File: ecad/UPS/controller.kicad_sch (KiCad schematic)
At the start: 32 parts, among them J4 Conn_01x05_Socket, SW1 SW_Push, SW2 SW_Push, U4 STM32L152RCT6, U5 AP2112K-3.3TRG1

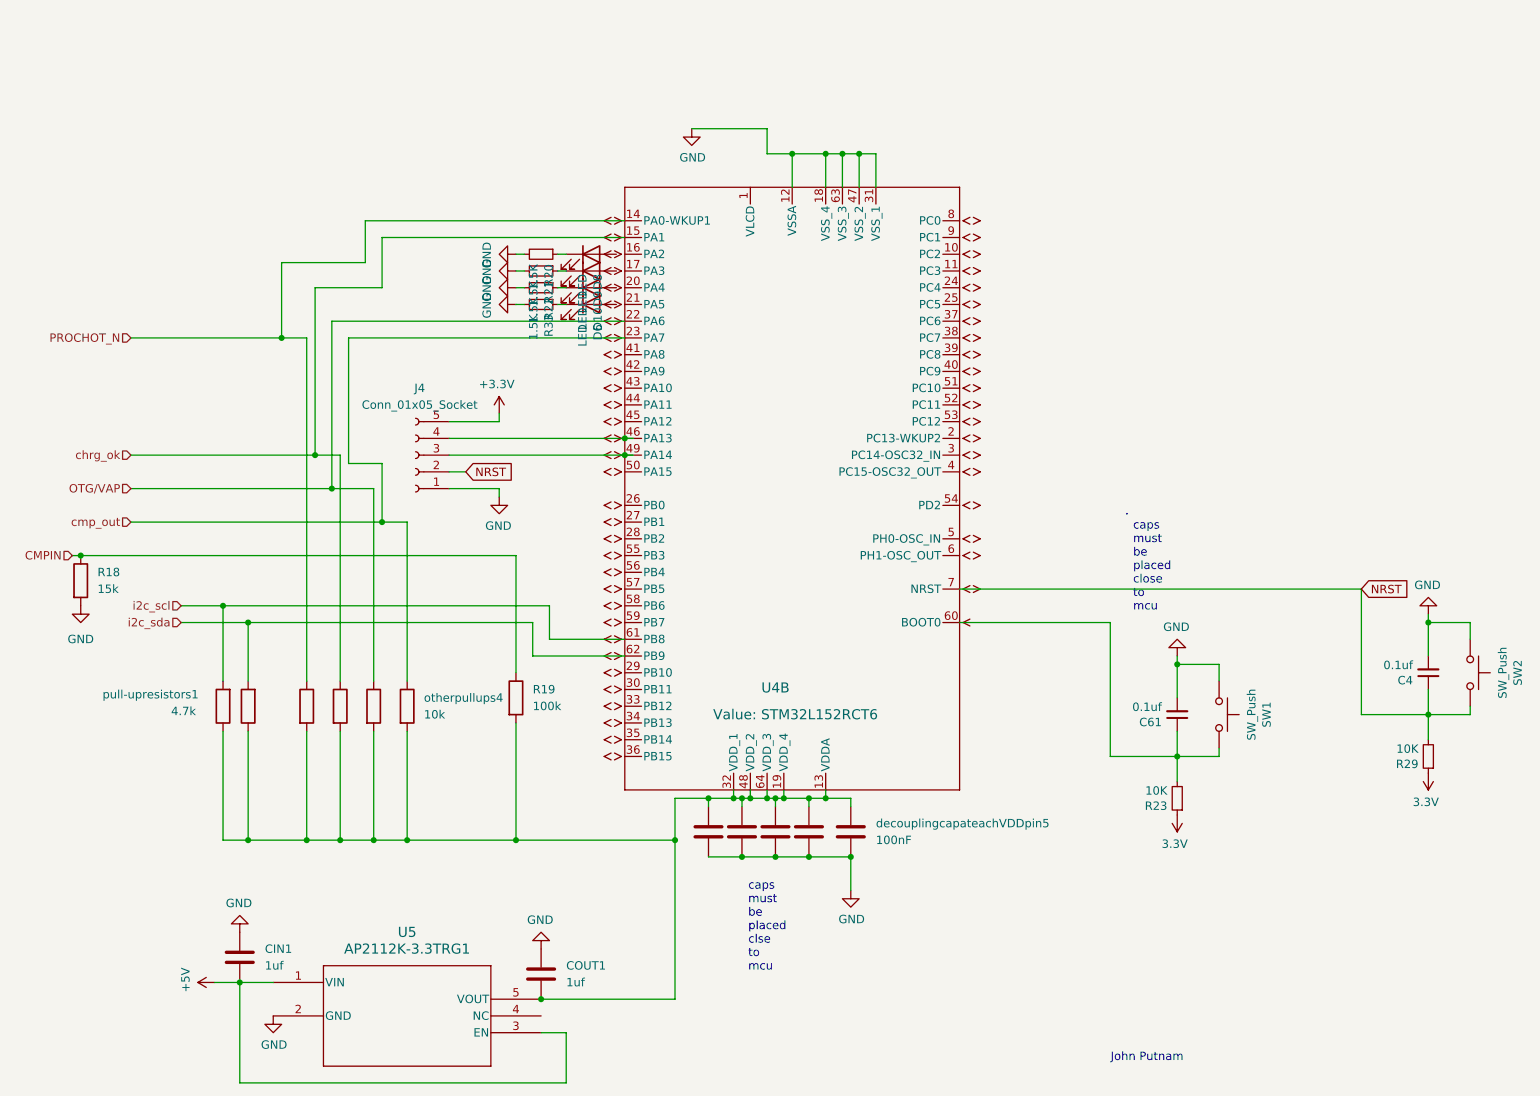
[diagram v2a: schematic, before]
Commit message: boot0 fix
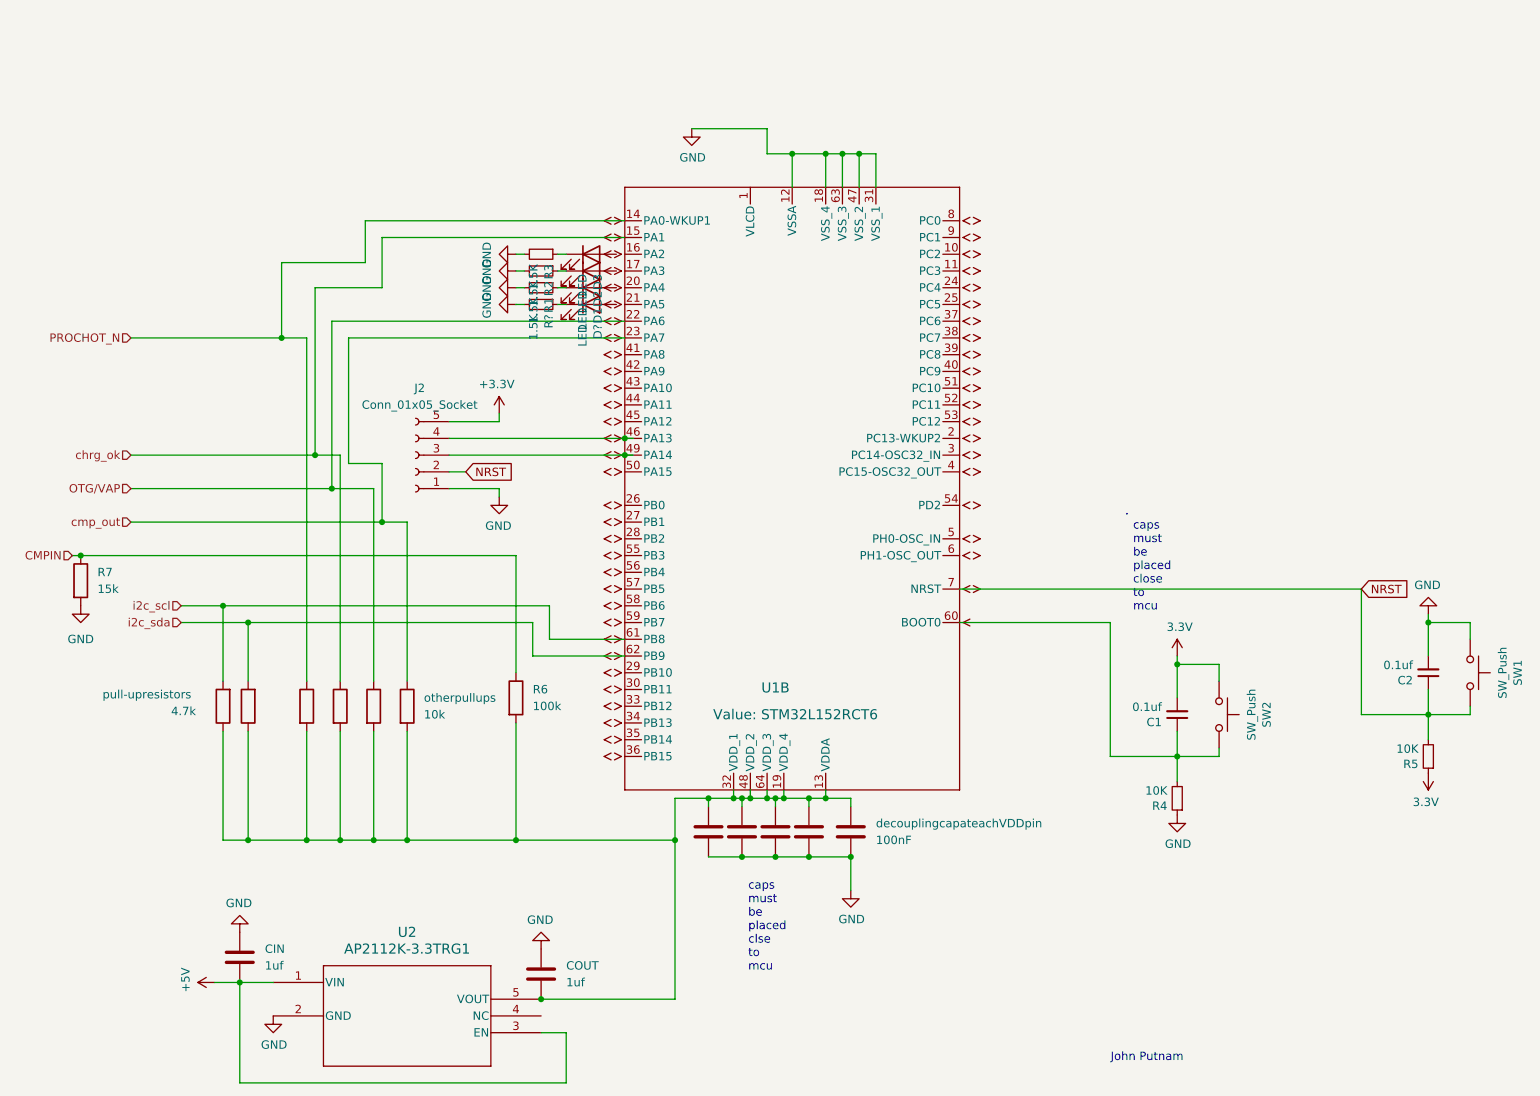
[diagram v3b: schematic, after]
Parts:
- renumbered C61 to C1, C4 to C2, CIN1 to CIN, COUT1 to COUT, D10 to D1, D9 to D2, D8 to D3, D6 to D?, J4 to J2, R22 to R1, R21 to R2, R20 to R3, R23 to R4, R29 to R5, R19 to R6, R18 to R7, R33 to R?, SW2 to SW1, SW1 to SW2, U4 to U1, U5 to U2, decouplingcapateachVDDpin5 to decouplingcapateachVDDpin, decouplingcapateachVDDpin4 to decouplingcapateachVDDpin1, decouplingcapateachVDDpin3 to decouplingcapateachVDDpin2, decouplingcapateachVDDpin2 to decouplingcapateachVDDpin3, decouplingcapateachVDDpin1 to decouplingcapateachVDDpin4, otherpullups4 to otherpullups, otherpullups3 to otherpullups1, otherpullups1 to otherpullups3, pull-upresistoronSDA1 to pull-upresistoronSDA, pull-upresistors1 to pull-upresistors
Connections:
- net 3.3V: now also C1.2, SW2.1; no longer R4.1
- net GND: now also R4.1; no longer C1.2, SW2.1
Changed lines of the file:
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@@
 		(on_board yes)
 		(dnp no)
-		(property "Reference" "#PWR0120"
+		(property "Reference" "#PWR030"
 			(at 87.63 78.74 0)
 			(effects
@@
 		(on_board yes)
 		(dnp no)
-		(property "Reference" "#PWR0126"
+		(property "Reference" "#PWR031"
 			(at 87.63 93.98 0)
 			(effects
@@
 		(on_board yes)
 		(dnp no)
-		(property "Reference" "#PWR0118"
+		(property "Reference" "#PWR012"
 			(at 48.26 161.29 0)
 			(effects
@@
 		(on_board yes)
 		(dnp no)
-		(property "Reference" "#PWR0119"
+		(property "Reference" "#PWR013"
 			(at 48.26 147.32 0)
 			(effects
@@
 		(on_board yes)
 		(dnp no)
-		(property "Reference" "#PWR0113"
+		(property "Reference" "#PWR04"
 			(at 228.6 125.73 0)
 			(effects
@@
 		(on_board yes)
 		(dnp no)
-		(property "Reference" "SW2"
+		(property "Reference" "SW1"
 			(at 242.189 114.3 0)
 			(effects
@@
 		(on_board yes)
 		(dnp no)
-		(property "Reference" "#PWR0114"
+		(property "Reference" "#PWR05"
 			(at 228.6 99.06 0)
 			(effects
@@
 		(on_board yes)
 		(dnp no)
-		(property "Reference" "#PWR0124"
+		(property "Reference" "#PWR024"
 			(at 83.82 58.42 0)
 			(effects
@@
 		(on_board yes)
 		(dnp no)
-		(property "Reference" "pull-upresistors1"
+		(property "Reference" "pull-upresistors"
 			(at 27.432 117.602 0)
 			(effects
@@
 		(on_board yes)
 		(dnp no)
-		(property "Reference" "D6"
+		(property "Reference" "D?"
 			(at 102.5906 61.4172 90)
 			(effects
@@
 		(dnp no)
 		(fields_autoplaced yes)
-		(property "Reference" "decouplingcapateachVDDpin4"
+		(property "Reference" "decouplingcapateachVDDpin1"
 			(at 138.43 137.1599 0)
 			(effects
@@
 		(on_board yes)
 		(dnp no)
-		(property "Reference" "C61"
+		(property "Reference" "C1"
 			(at 188.1632 121.8184 0)
 			(effects
@@
 		(on_board yes)
 		(dnp no)
-		(property "Reference" "R29"
+		(property "Reference" "R5"
 			(at 227.1014 128.1684 0)
 			(effects
@@
 		(on_board yes)
 		(dnp no)
-		(property "Reference" "R21"
+		(property "Reference" "R2"
 			(at 95.1484 54.8386 0)
 			(effects
@@
 		(on_board yes)
 		(dnp no)
-		(property "Reference" "D9"
+		(property "Reference" "D2"
 			(at 102.5906 56.3372 90)
 			(effects
@@
 		(dnp no)
 		(fields_autoplaced yes)
-		(property "Reference" "decouplingcapateachVDDpin5"
+		(property "Reference" "decouplingcapateachVDDpin"
 			(at 144.78 137.1599 0)
 			(effects
@@
 		(on_board yes)
 		(dnp no)
-		(property "Reference" "R33"
+		(property "Reference" "R?"
 			(at 95.1484 59.9186 0)
 			(effects
@@
 		(on_board yes)
 		(dnp no)
-		(property "Reference" "R22"
+		(property "Reference" "R1"
 			(at 95.1484 57.3786 0)
 			(effects
@@
 	(symbol
 		(lib_id "power:+3.3V")
-		(at 190.5 135.89 180)
+		(at 190.5 111.76 0)
 		(unit 1)
 		(exclude_from_sim no)
@@
 		(on_board yes)
 		(dnp no)
-		(property "Reference" "#PWR0110"
-			(at 190.5 132.08 0)
+		(property "Reference" "#PWR014"
+			(at 190.5 115.57 0)
 			(effects
 				(font
@@
 		)
 		(property "Value" "3.3V"
-			(at 190.119 140.2842 0)
+			(at 190.881 107.3658 0)
 			(effects
 				(font
@@
 		)
 		(property "Footprint" ""
-			(at 190.5 135.89 0)
+			(at 190.5 111.76 0)
 			(effects
 				(font
@@
 		)
 		(property "Datasheet" ""
-			(at 190.5 135.89 0)
+			(at 190.5 111.76 0)
 			(effects
 				(font
@@
 		)
 		(property "Description" ""
-			(at 190.5 135.89 0)
+			(at 190.5 111.76 0)
 			(effects
 				(font
@@
 				)
 			)
-			(project "UPS"
-				(path "/9d92b60a-4a6b-449c-b462-cab19e69d38c/1d606685-c4fd-4b8c-9a71-b1626d28c437"
-					(reference "#PWR0110")
-					(unit 1)
-				)
-			)
 		)
 	)
@@
 		(on_board yes)
 		(dnp no)
-		(property "Reference" "#PWR0121"
+		(property "Reference" "#PWR09"
 			(at 83.82 50.8 0)
 			(effects
@@
 		(dnp no)
 		(fields_autoplaced yes)
-		(property "Reference" "R18"
+		(property "Reference" "R7"
 			(at 26.67 99.0599 0)
 			(effects
@@
 		(on_board yes)
 		(dnp no)
-		(property "Reference" "#PWR0123"
+		(property "Reference" "#PWR07"
 			(at 83.82 55.88 0)
 			(effects
@@
 		(on_board yes)
 		(dnp no)
-		(property "Reference" "#PWR0111"
+		(property "Reference" "#PWR06"
 			(at 140.97 153.67 0)
 			(effects
@@
 		(dnp no)
 		(fields_autoplaced yes)
-		(property "Reference" "U5"
+		(property "Reference" "U2"
 			(at 73.66 153.67 0)
 			(effects
@@
 		(on_board yes)
 		(dnp no)
-		(property "Reference" "#PWR0125"
+		(property "Reference" "#PWR010"
 			(at 116.84 38.1 0)
 			(effects
@@
 		(on_board yes)
 		(dnp no)
-		(property "Reference" "SW1"
+		(property "Reference" "SW2"
 			(at 204.089 120.65 0)
 			(effects
@@
 		(on_board yes)
 		(dnp no)
-		(property "Reference" "#PWR0116"
+		(property "Reference" "#PWR02"
 			(at 53.34 172.72 0)
 			(effects
@@
 		(on_board yes)
 		(dnp no)
-		(property "Reference" "D8"
+		(property "Reference" "D3"
 			(at 102.5906 53.7972 90)
 			(effects
@@
 		(on_board yes)
 		(dnp no)
-		(property "Reference" "D10"
+		(property "Reference" "D1"
 			(at 102.5906 58.8772 90)
 			(effects
@@
 		(dnp no)
 		(fields_autoplaced yes)
-		(property "Reference" "otherpullups4"
+		(property "Reference" "otherpullups"
 			(at 76.2 118.1099 0)
 			(effects
@@
 		(dnp no)
 		(fields_autoplaced yes)
-		(property "Reference" "otherpullups3"
+		(property "Reference" "otherpullups1"
 			(at 71.12 118.1099 0)
 			(effects
@@
 		(dnp no)
 		(fields_autoplaced yes)
-		(property "Reference" "pull-upresistoronSDA1"
+		(property "Reference" "pull-upresistoronSDA"
 			(at 52.07 118.1099 0)
 			(effects
@@
 		(dnp no)
 		(fields_autoplaced yes)
-		(property "Reference" "J4"
+		(property "Reference" "J2"
 			(at 75.565 71.12 0)
 			(effects
@@
 		(dnp no)
 		(fields_autoplaced yes)
-		(property "Reference" "decouplingcapateachVDDpin2"
+		(property "Reference" "decouplingcapateachVDDpin3"
 			(at 128.27 137.1599 0)
 			(effects
@@
 		(on_board yes)
 		(dnp no)
-		(property "Reference" "R23"
+		(property "Reference" "R4"
 			(at 189.0014 134.5184 0)
 			(effects
@@
 	(symbol
 		(lib_id "power:GND")
-		(at 190.5 111.76 180)
+		(at 190.5 135.89 0)
 		(unit 1)
 		(exclude_from_sim no)
@@
 		(on_board yes)
 		(dnp no)
-		(property "Reference" "#PWR0112"
-			(at 190.5 105.41 0)
+		(property "Reference" "#PWR011"
+			(at 190.5 142.24 0)
 			(effects
 				(font
@@
 		)
 		(property "Value" "GND"
-			(at 190.373 107.3658 0)
+			(at 190.627 140.2842 0)
 			(effects
 				(font
@@
 		)
 		(property "Footprint" ""
-			(at 190.5 111.76 0)
+			(at 190.5 135.89 0)
 			(effects
 				(font
@@
 		)
 		(property "Datasheet" ""
-			(at 190.5 111.76 0)
+			(at 190.5 135.89 0)
 			(effects
 				(font
@@
 		)
 		(property "Description" ""
-			(at 190.5 111.76 0)
+			(at 190.5 135.89 0)
 			(effects
 				(font
@@
 				)
 			)
-			(project "UPS"
-				(path "/9d92b60a-4a6b-449c-b462-cab19e69d38c/1d606685-c4fd-4b8c-9a71-b1626d28c437"
-					(reference "#PWR0112")
-					(unit 1)
-				)
-			)
 		)
 	)
@@
 		(dnp no)
 		(fields_autoplaced yes)
-		(property "Reference" "COUT1"
+		(property "Reference" "COUT"
 			(at 97.79 158.7499 0)
 			(effects
@@
 		(dnp no)
 		(fields_autoplaced yes)
-		(property "Reference" "R19"
+		(property "Reference" "R6"
 			(at 92.71 116.8399 0)
 			(effects
@@
 		(dnp no)
 		(fields_autoplaced yes)
-		(property "Reference" "otherpullups1"
+		(property "Reference" "otherpullups3"
 			(at 60.96 118.1099 0)
 			(effects
@@
 		(on_board yes)
 		(dnp no)
-		(property "Reference" "C4"
+		(property "Reference" "C2"
 			(at 226.2632 115.4684 0)
 			(effects
@@
 		(dnp no)
 		(fields_autoplaced yes)
-		(property "Reference" "CIN1"
+		(property "Reference" "CIN"
 			(at 52.07 156.2099 0)
 			(effects
@@
 		(on_board yes)
 		(dnp no)
-		(property "Reference" "R20"
+		(property "Reference" "R3"
 			(at 95.1484 52.2986 0)
 			(effects
@@
 		(dnp no)
 		(fields_autoplaced yes)
-		(property "Reference" "decouplingcapateachVDDpin1"
+		(property "Reference" "decouplingcapateachVDDpin4"
 			(at 123.19 137.1599 0)
 			(effects
@@
 		(on_board yes)
 		(dnp no)
-		(property "Reference" "#PWR0115"
+		(property "Reference" "#PWR01"
 			(at 93.98 149.86 0)
 			(effects
@@
 		(dnp no)
 		(fields_autoplaced yes)
-		(property "Reference" "decouplingcapateachVDDpin3"
+		(property "Reference" "decouplingcapateachVDDpin2"
 			(at 133.35 137.1599 0)
 			(effects
@@
 		(on_board yes)
 		(dnp no)
-		(property "Reference" "U4"
+		(property "Reference" "U1"
 			(at 129.54 116.586 0)
 			(effects
@@
 		(dnp no)
 		(fields_autoplaced yes)
-		(property "Reference" "#PWR0109"
+		(property "Reference" "#PWR03"
 			(at 24.13 110.49 0)
 			(effects
@@
 		(on_board yes)
 		(dnp no)
-		(property "Reference" "#PWR0122"
+		(property "Reference" "#PWR08"
 			(at 83.82 53.34 0)
 			(effects

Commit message: minor things
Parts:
- removed J2: Conn_01x05_Socket, symbol Connector:Conn_01x05_Socket
- added J2: PROG, Connector_PinHeader_2.54mm:PinHeader_1x04_P2.54mm_Vertical, symbol Connector_Generic:Conn_01x04
- gave numbers to parts that had none: 2
- renumbered D3 to D4, R3 to R4
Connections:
- net +3.3V: now also J2.1 (Pin_1)
- net GND: now also D1.1 (K), R1.1, J2.4 (Pin_4)
- net at D1.2 (A): now also U1.21 (PA5)
- net at D2.2 (A): now also U1.17 (PA3)
- net at D4.2 (A): now also U1.16 (PA2)
- net at D1.2 (A): now also U1.20 (PA4)
- net PA14_SWCLK: now reaches U1.49 (PA14)
- net PA14_SWCLK: now also J2.3 (Pin_3)
- net PA13_SWDIO: now reaches U1.46 (PA13)
- net PA13_SWDIO: now also J2.2 (Pin_2)
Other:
- moved on the sheet: D1, R1
